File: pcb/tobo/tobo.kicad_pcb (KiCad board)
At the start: 2 copper layers, 57.5 x 61 mm, 87 parts, among them J2 Conn_01x02_Pin, J4 54548-2472, J5 Conn_01x09_Pin, J6 Conn_01x09_Pin, J7 Conn_01x09_Pin, J8 Hroparts Elec TYPE-C-31-M-12, U1 TS5A23167DCUR, U10 5015, U11 5015, U12 5015, U13 5015, U14 CH340E, U15 5015, U16 5015, U2 ATmega328P-AN, U3 TS5A23167DCUR, U4 TS5A23167DCUR, U5 TS5A23167DCUR, U6 5015, U7 5015, U8 5015, U9 5015, X1 TestPoint, X2 TestPoint, X7 TestPoint, Y4 TestPoint

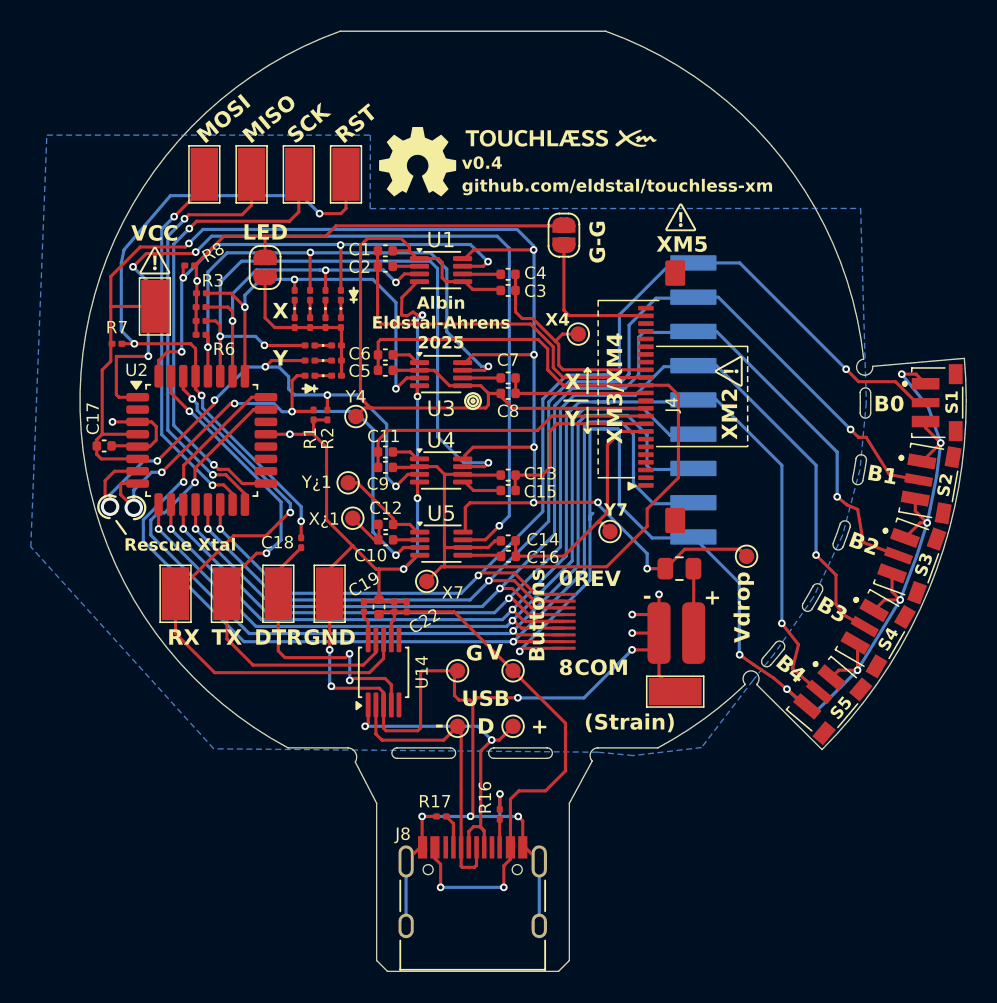
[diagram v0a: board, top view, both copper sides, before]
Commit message: First stab at a step-up converter on the tobo
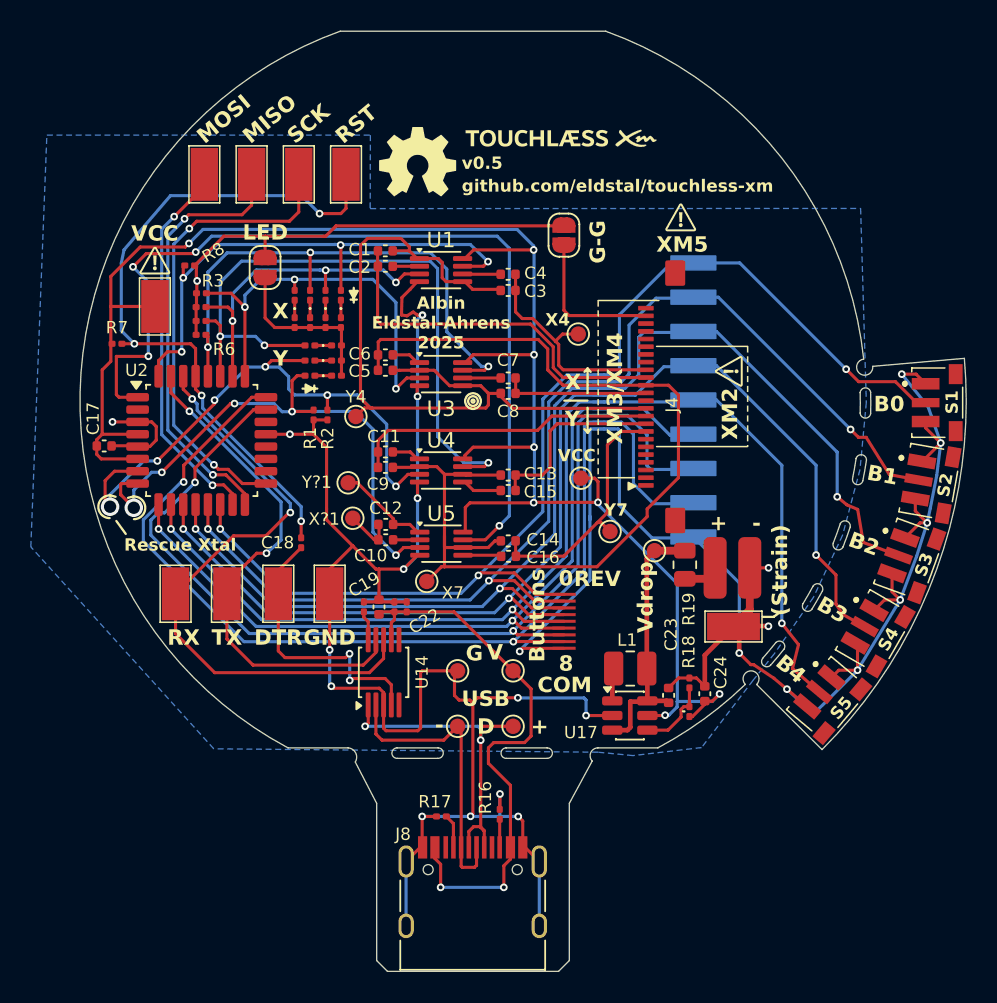
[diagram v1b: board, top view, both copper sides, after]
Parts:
- added C23: 10uF, Capacitor_SMD:C_0402_1005Metric, F.Cu at (152.7, 109.1)
- added C24: 10uF, Capacitor_SMD:C_0402_1005Metric, F.Cu at (155.0, 109.0)
- added L1: 4.7uH, Inductor_SMD:L_1008_2520Metric, F.Cu at (150.2, 107.4)
- added R18: 1M, Resistor_SMD:R_0201_0603Metric, F.Cu at (154.0, 110.1)
- added R19: 180k, Resistor_SMD:R_0201_0603Metric, F.Cu at (154.0, 108.3)
- added U17: TLV61220ADBVR, Package_TO_SOT_SMD:SOT-23-6, F.Cu at (150.2, 110.4)
- added V2: TestPoint, TestPoint:TestPoint_Pad_D1.0mm, F.Cu at (147.0, 95.0)
- moved V1 5.98 mm to (151.8, 99.7)
- moved U13 5.67 mm to (156.9, 104.6)
- moved J2 5.58 mm to (159.0, 101.6)
- moved R27 0.43 mm to (153.7, 100.6), turned to -90 degrees
- renumbered X¿1 to X?1, Y¿1 to Y?1
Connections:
- C17 pad 2: +BATT -> VCC
- R7 pad 1: +BATT -> VCC
- U1 pad 8: +BATT -> VCC
- U15 pad 1: +BATT -> VCC
- U2 pad 4: +BATT -> VCC
- U2 pad 6: +BATT -> VCC
- U3 pad 8: +BATT -> VCC
- U4 pad 8: +BATT -> VCC
- U5 pad 8: +BATT -> VCC
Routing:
- net VCC: track 0.00 -> 115.8 mm, vias 0 -> 8
- net +BATT: track 102.9 -> 17.8 mm, vias 7 -> 0
- net Net-(U17-FB): track 0.00 -> 4.87 mm
- net GND: track 259.4 -> 262.3 mm, vias 26 -> 25
- net Net-(U17-SW): track 0.00 -> 2.14 mm
- net Net-(J2-Pin_2): track 4.19 -> 2.26 mm
- net Net-(U14-UD+): track 21.3 -> 21.9 mm
- net Net-(U14-VCC): track 36.9 -> 36.4 mm
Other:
- outline, holes or cut-outs redrawn
- board text added: "v0.5"
- board text removed: "v0.4"

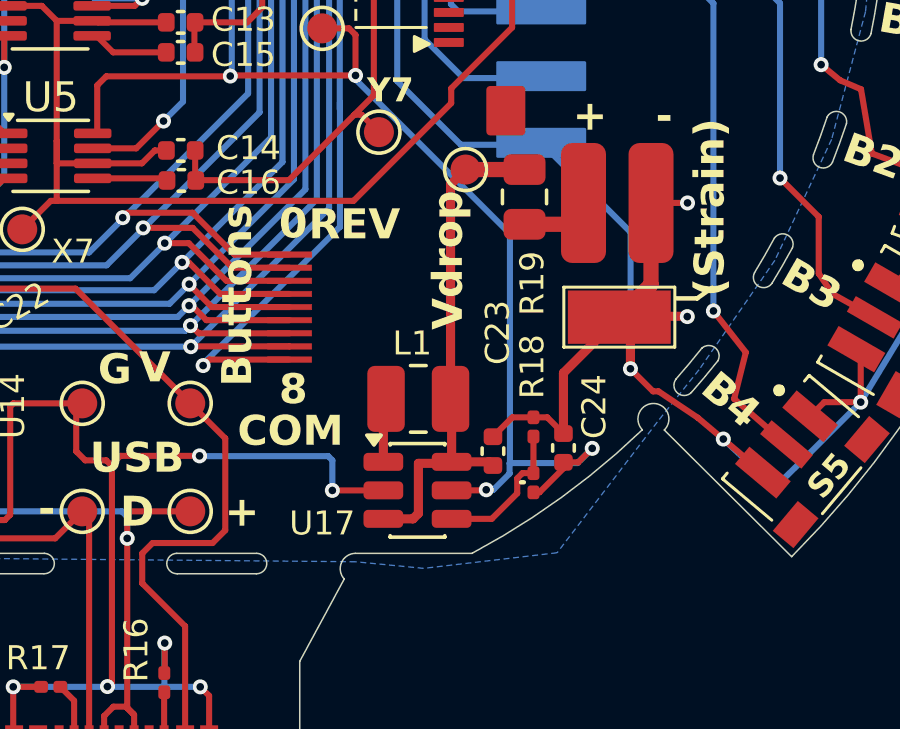
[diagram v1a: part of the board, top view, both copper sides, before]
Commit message: Half-way to a better transformer
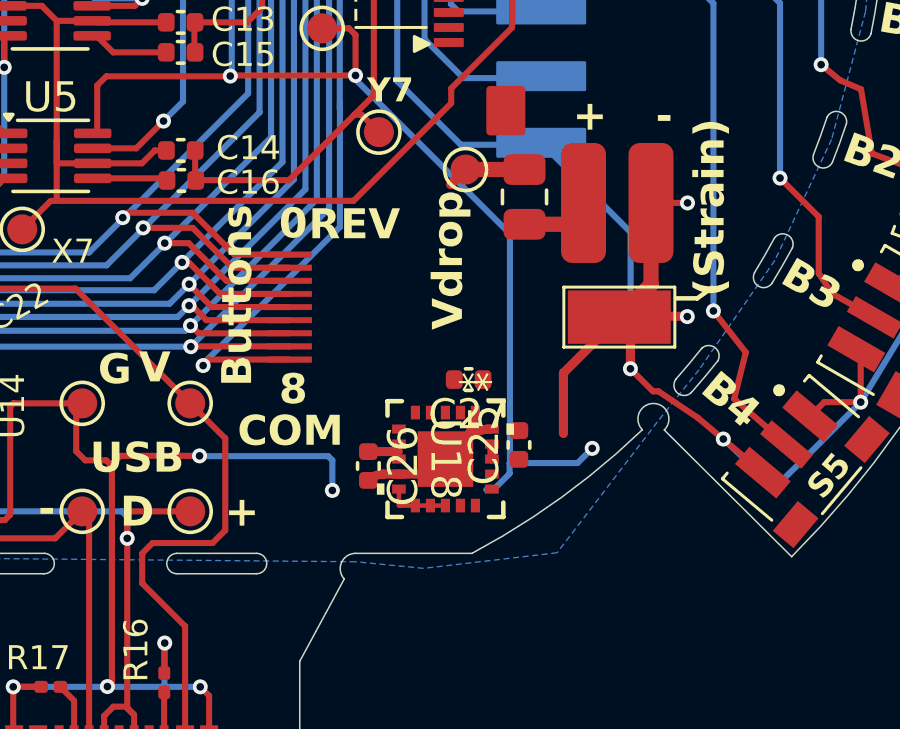
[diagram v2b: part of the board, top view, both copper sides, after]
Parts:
- removed C23, C24: 10uF, Capacitor_SMD:C_0402_1005Metric
- removed L1: 4.7uH, Inductor_SMD:L_1008_2520Metric
- removed R18: 1M, Resistor_SMD:R_0201_0603Metric
- removed R19: 180k, Resistor_SMD:R_0201_0603Metric
- removed U17: TLV61220ADBVR, Package_TO_SOT_SMD:SOT-23-6
- added C25: 10uF, Capacitor_SMD:C_0402_1005Metric, F.Cu at (153.6, 108.9)
- added C26: 22uF, Capacitor_SMD:C_0402_1005Metric, F.Cu at (148.5, 109.6)
- added C27: 2.2uF, Capacitor_SMD:C_0402_1005Metric, F.Cu at (151.9, 106.7)
- added U18: MAXM20343AMP+, tobo-footprints:21-100447_ADI, F.Cu at (151.1, 109.4)
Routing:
- net +BATT: track 17.8 -> 4.54 mm
- net Net-(U17-FB): track 4.87 -> 0.00 mm
- net VCC: track 115.8 -> 112.5 mm, vias 8 -> 7
- net Net-(U17-SW): track 2.14 -> 0.00 mm
- net Net-(U18-HVLX-Pad12): track 0.00 -> 2.10 mm
- net GND: track 262.3 -> 261.7 mm

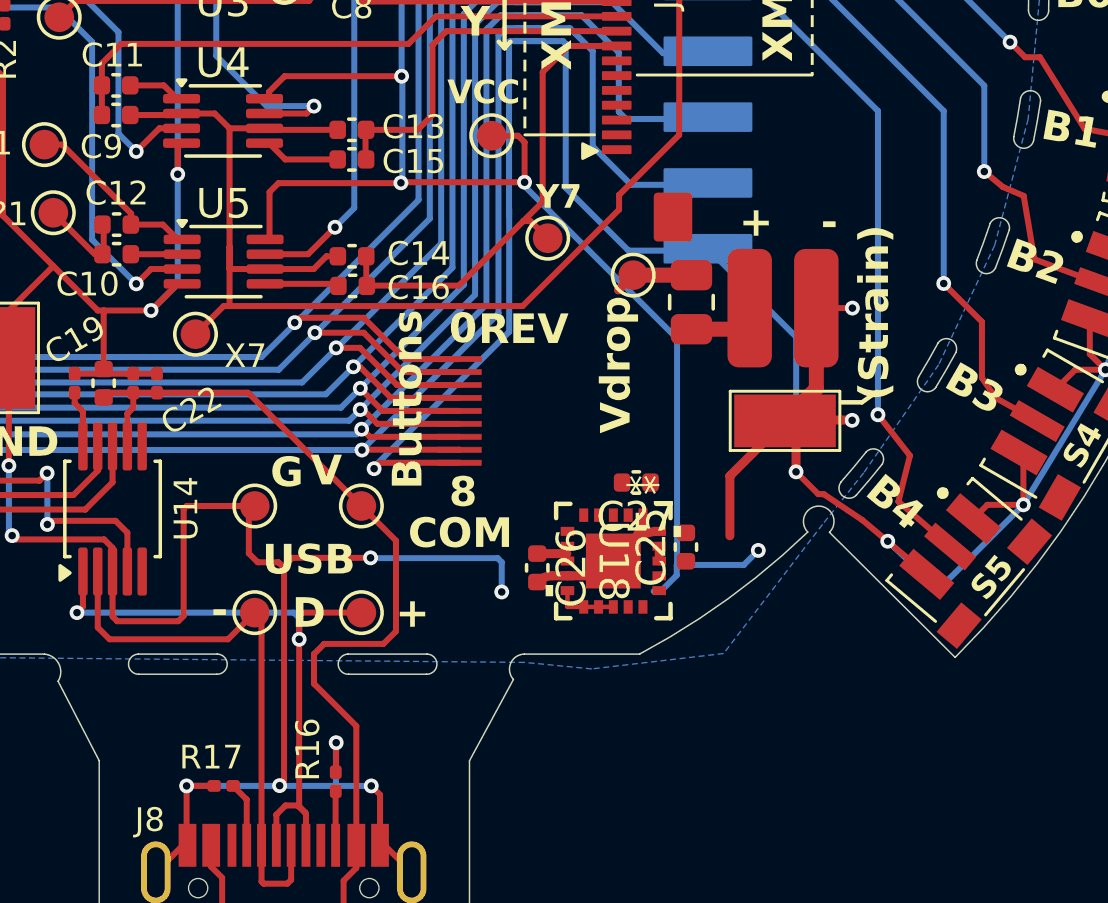
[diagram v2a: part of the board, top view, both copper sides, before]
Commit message: A mostly one-chip up- and down- converter.
This should work down to 0.5V, which is just a little bit over the low
battery warning of the headset.
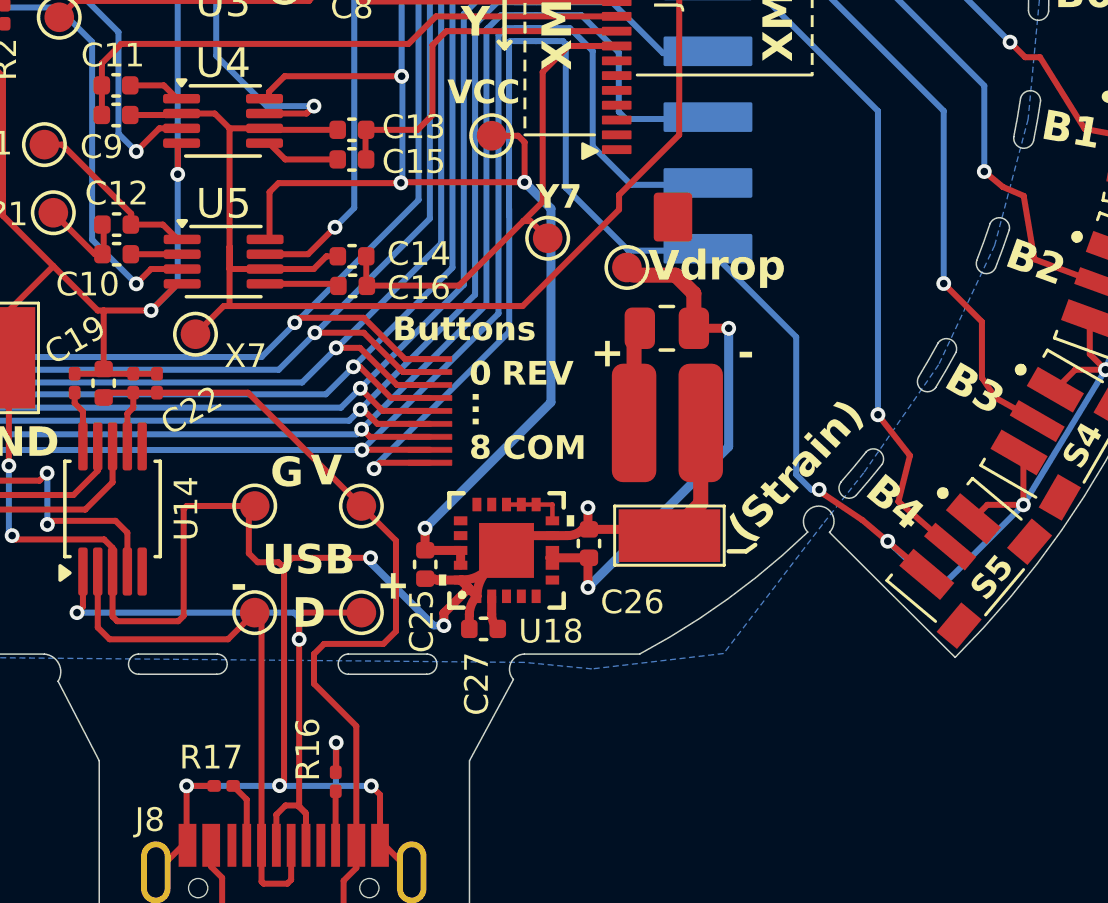
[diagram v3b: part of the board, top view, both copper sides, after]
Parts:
- moved C25 8.82 mm to (144.8, 109.5), turned to -90 degrees
- moved C27 7.14 mm to (146.7, 111.6), turned to 0 degrees
- moved J2 5.50 mm to (155.1, 105.4)
- moved U13 5.50 mm to (153.0, 108.5)
- moved U18 3.62 mm to (147.5, 109.0), turned to 90 degrees
- moved C26 1.93 mm to (150.3, 108.8), turned to 90 degrees
- moved R27 1.21 mm to (152.9, 101.5), turned to 180 degrees
- moved J7 0.99 mm to (144.2, 104.3)
- moved V1 0.34 mm to (151.6, 99.4)
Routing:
- net +BATT: track 4.54 -> 17.7 mm, vias 0 -> 2
- net GND: track 261.7 -> 257.0 mm, vias 25 -> 24
- net VCC: track 112.5 -> 108.7 mm
- net Net-(U18-CAP): track 0.00 -> 1.15 mm
- net /BTN3: track 75.3 -> 74.3 mm
- net Net-(J2-Pin_2): track 2.26 -> 3.28 mm
- net /BTN6: track 67.2 -> 66.2 mm
- net /BTN5: track 54.3 -> 53.3 mm
- net /BTN4: track 76.2 -> 75.2 mm
- net /BTN2: track 75.9 -> 74.9 mm
- net /BTN1: track 74.6 -> 73.6 mm
- net /BTN0: track 74.3 -> 73.3 mm
- net /BTN7: track 70.5 -> 69.5 mm
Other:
- board text added: "..."

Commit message: Minor versioning shenanigans
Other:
- board text added: "v0.5a"
- board text removed: "v0.5"
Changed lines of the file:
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@@
 			)
 		)
-		(property "Manufacturer_Part_Number" ""
+		(property "Manufacturer_Part_Number" "CL05A226MQ5QUNC"
 			(at 0 0 90)
 			(unlocked yes)
@@
 			)
 		)
-		(property "LCSC Part Number" ""
+		(property "LCSC Part Number" "C105226"
 			(at 0 0 90)
 			(unlocked yes)
@@
 			)
 		)
-		(property "Manufacturer_Part_Number" ""
+		(property "Manufacturer_Part_Number" "CL05A225KO5NQNC"
 			(at 0 0 0)
 			(unlocked yes)
@@
 			)
 		)
-		(property "LCSC Part Number" ""
+		(property "LCSC Part Number" "C170151"
 			(at 0 0 0)
 			(unlocked yes)
@@
 		)
 	)
-	(gr_text "v0.5"
+	(gr_text "v0.5a"
 		(at 139.267504 75.028047 0)
 		(layer "F.SilkS")

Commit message: Sync commit
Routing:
- net GND: track 257.0 -> 262.3 mm, vias 24 -> 27
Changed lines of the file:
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@@
+	)
+	(segment
+		(start 154.056765 104.695273)
+		(end 155.111492 105.75)
+		(width 0.3048)
+		(layer "F.Cu")
+		(net 26)
 	)
 	(segment
@@
 	)
 	(segment
+		(start 155.111492 105.75)
+		(end 155.5 105.75)
+		(width 0.3048)
+		(layer "F.Cu")
+		(net 26)
+	)
+	(segment
 		(start 122.08 82.98)
 		(end 122.06 83)
@@
 	)
 	(segment
+		(start 155.500073 104.695273)
+		(end 155.5548 104.75)
+		(width 0.1524)
+		(layer "F.Cu")
+		(net 26)
+	)
+	(segment
 		(start 136.7 116.95)
 		(end 136.7 118.925)
@@
 	)
 	(segment
+		(start 155.002038 103.75)
+		(end 155.5548 103.75)
+		(width 0.3048)
+		(layer "F.Cu")
+		(net 26)
+	)
+	(segment
 		(start 166.028751 103.571972)
 		(end 166.700996 102.899727)
@@
 		(end 133.9 100.9)
 		(width 0.2032)
+		(layer "F.Cu")
+		(net 26)
+	)
+	(segment
+		(start 154.056765 104.695273)
+		(end 155.002038 103.75)
+		(width 0.3048)
 		(layer "F.Cu")
 		(net 26)
@@
 	)
 	(segment
+		(start 154.056765 104.695273)
+		(end 155.500073 104.695273)
+		(width 0.3048)
+		(layer "F.Cu")
+		(net 26)
+	)
+	(segment
 		(start 145.999999 110.000001)
 		(end 146 110)
@@
 	)
 	(via
+		(at 155.5548 103.75)
+		(size 0.5)
+		(drill 0.254)
+		(layers "F.Cu" "B.Cu")
+		(net 26)
+	)
+	(via
 		(at 122.1 82.2)
 		(size 0.5)
@@
 	)
 	(via
+		(at 155.5 105.75)
+		(size 0.5)
+		(drill 0.254)
+		(layers "F.Cu" "B.Cu")
+		(net 26)
+	)
+	(via
 		(at 167.82 88.25)
 		(size 0.5)
@@
 		(size 0.5)
 		(drill 0.254)
+		(layers "F.Cu" "B.Cu")
+		(net 26)
+	)
+	(via
+		(at 155.5548 104.75)
+		(size 0.5)
+		(drill 0.254)
